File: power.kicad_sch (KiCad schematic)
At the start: 87 parts, among them Q1 BSS138AKA, Q2 SQS401EN-T1_BE3, Q3 BCM857BS-7-F, U3 LMR62014XMF, U4 AP62301_TSOT, U5 AP62301_TSOT, U6 AP22615A_TSOT26

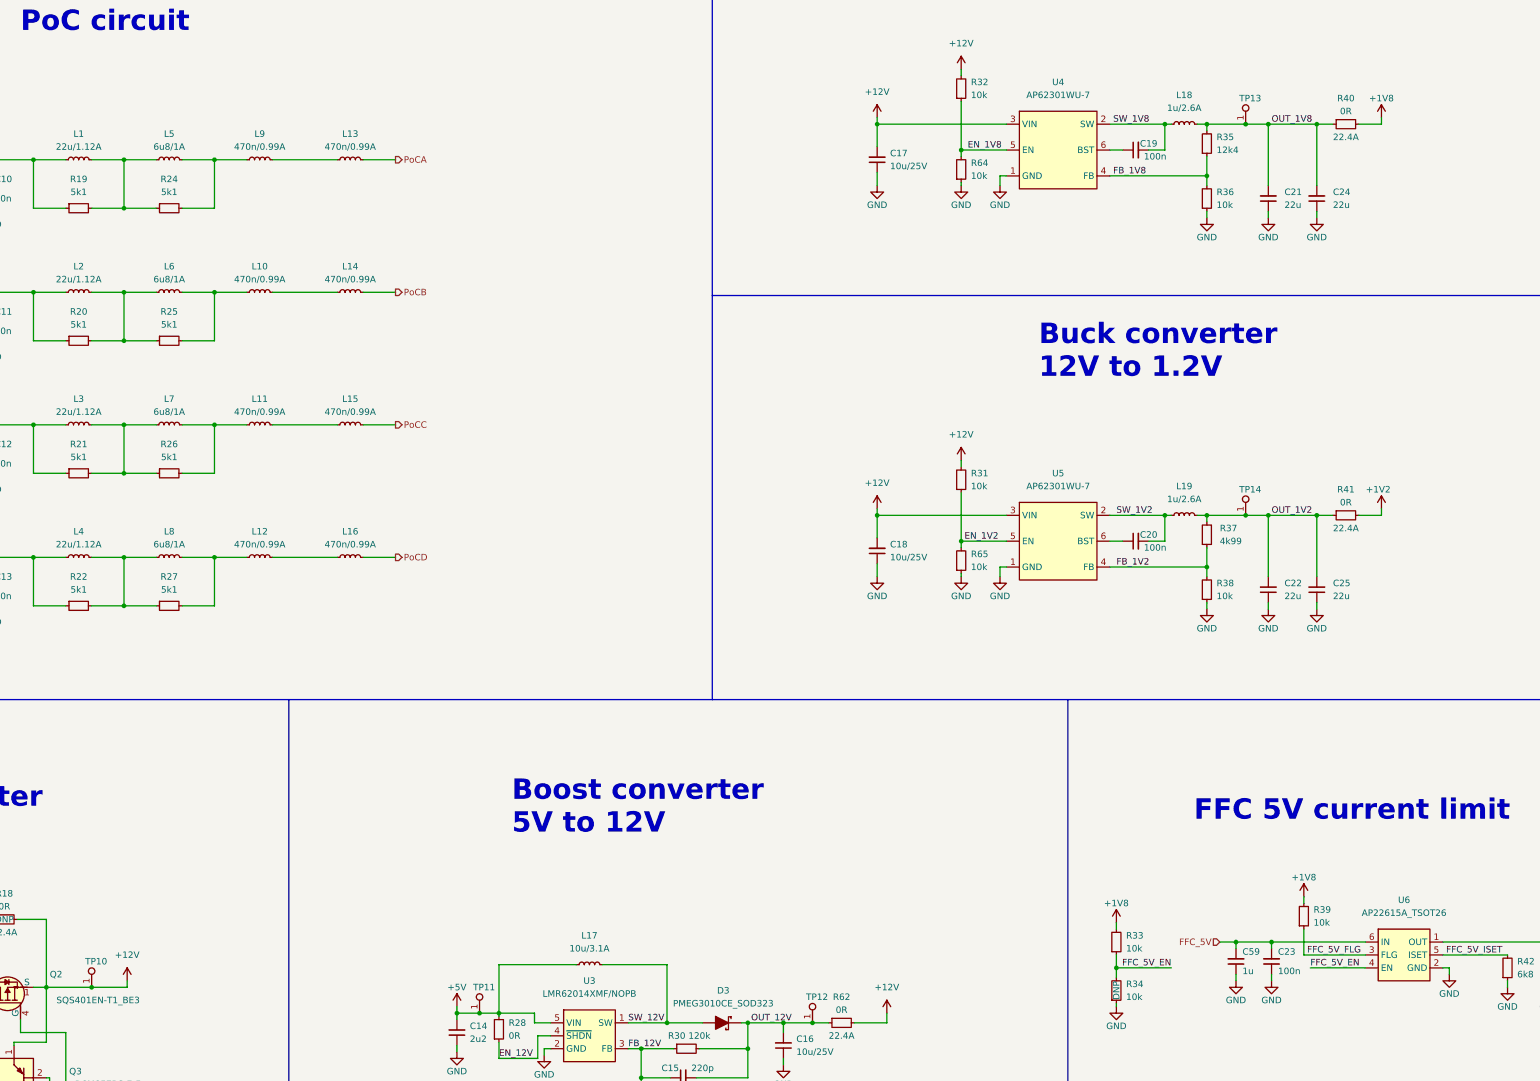
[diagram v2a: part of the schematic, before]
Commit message: Clean ERC, move LED from 5V to 12V
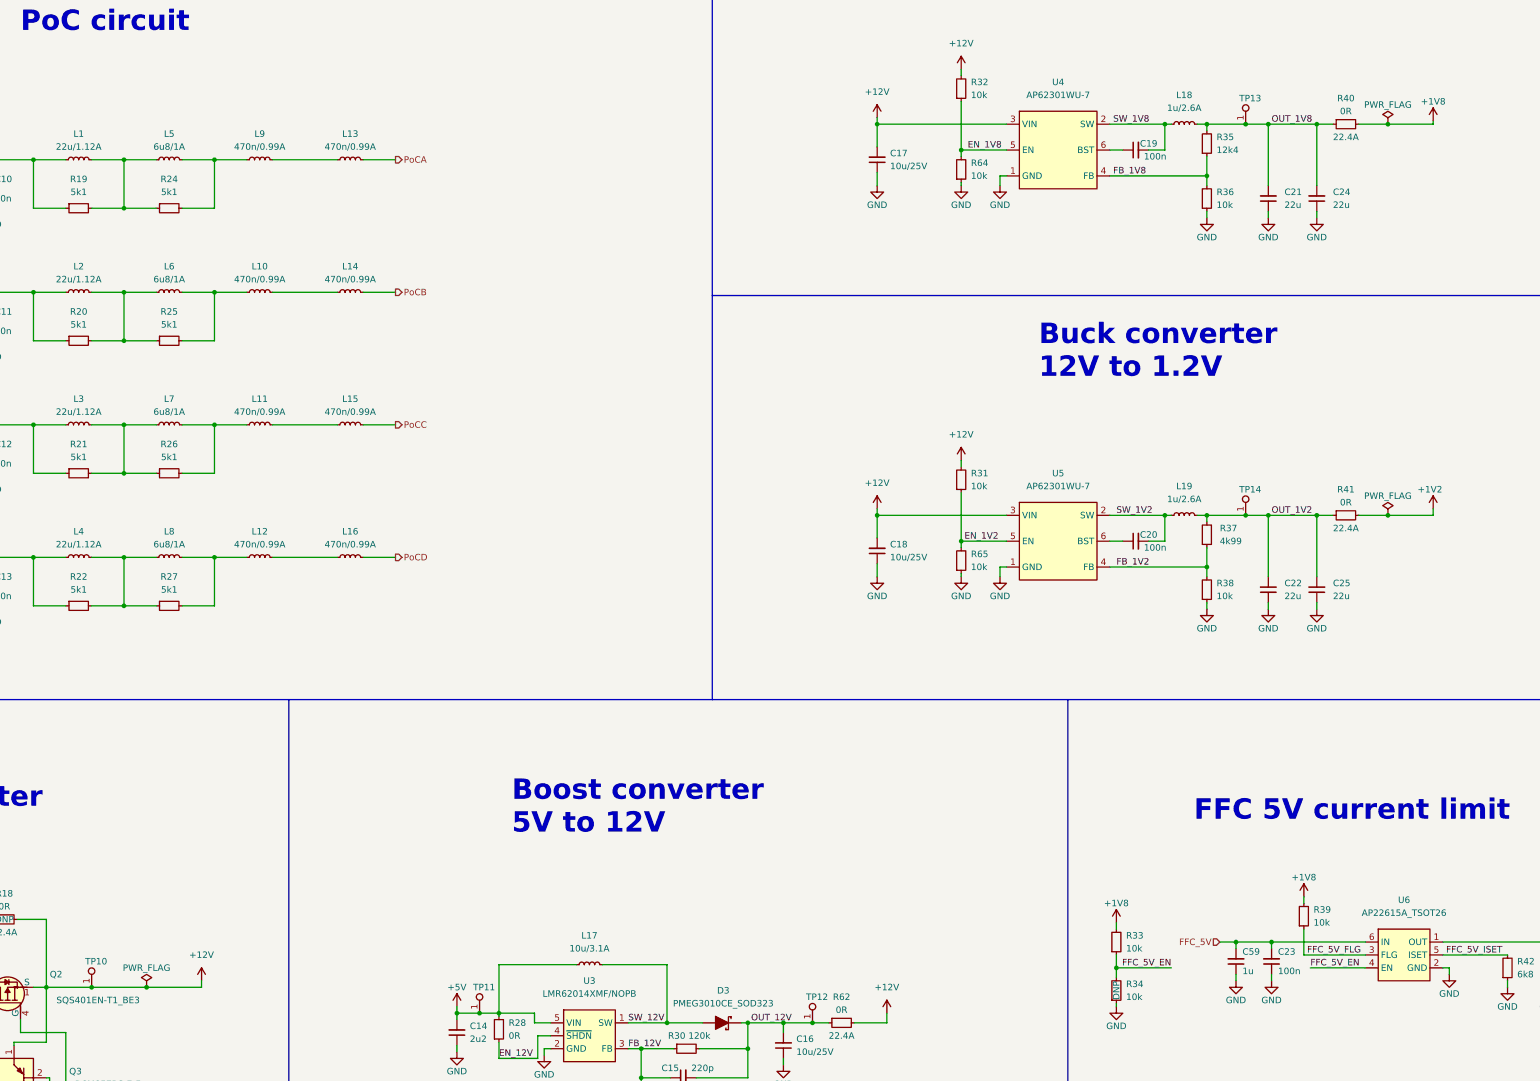
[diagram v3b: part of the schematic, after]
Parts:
- L1, L2, L3, L4: ISat 0.97A -> 1.12A
- L10, L11, L12, L13, L14, L15, L16, L9: ISat 0.76 A -> 0.99 A
- L5, L6, L7, L8: ISat 1.4 A -> 1 A
